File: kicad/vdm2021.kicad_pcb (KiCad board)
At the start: 2 copper layers, 254 x 134.1 mm, 177 parts, among them IC1 7406, IC10 74LS109, IC11 74LS138, IC12 74LS86, IC13 74LS109, IC14 74LS02, IC15 74LS00, IC16 74LS109, IC17 74LS175, IC18 74LS132, IC19 74LS04, IC2 74LS163, IC20 74LS163, IC21 74LS163, IC22 74LS163, IC23 74LS157, IC24 74LS157, IC25 4049, IC26 4029, IC27 4029, IC28 74LS157, IC29 DM8131, IC3 74166, IC30 4001, IC31 4042, IC32 4042, IC33 74LS08, IC34 74LS08, IC35 74LS00, IC36 74LS04, IC37 8836, IC38 74LS367, IC39 74LS367, IC4 MCM6575, IC40 74LS10, IC41 2102, IC42 2102, IC43 2102, IC44 2102, IC45 2102, IC46 2102, IC47 2102, IC48 2102, IC49 L7805, IC5 74LS175, IC50 L7812, IC6 74LS175, IC7 74LS20, IC8 93L16, IC9 74LS10, J2 Jumper_3_Open, J4 Jumper_2_Open, J5 Jumper_2_Open, Q1 2N2907, SW1 SW_DIP_x06, Y1 Crystal

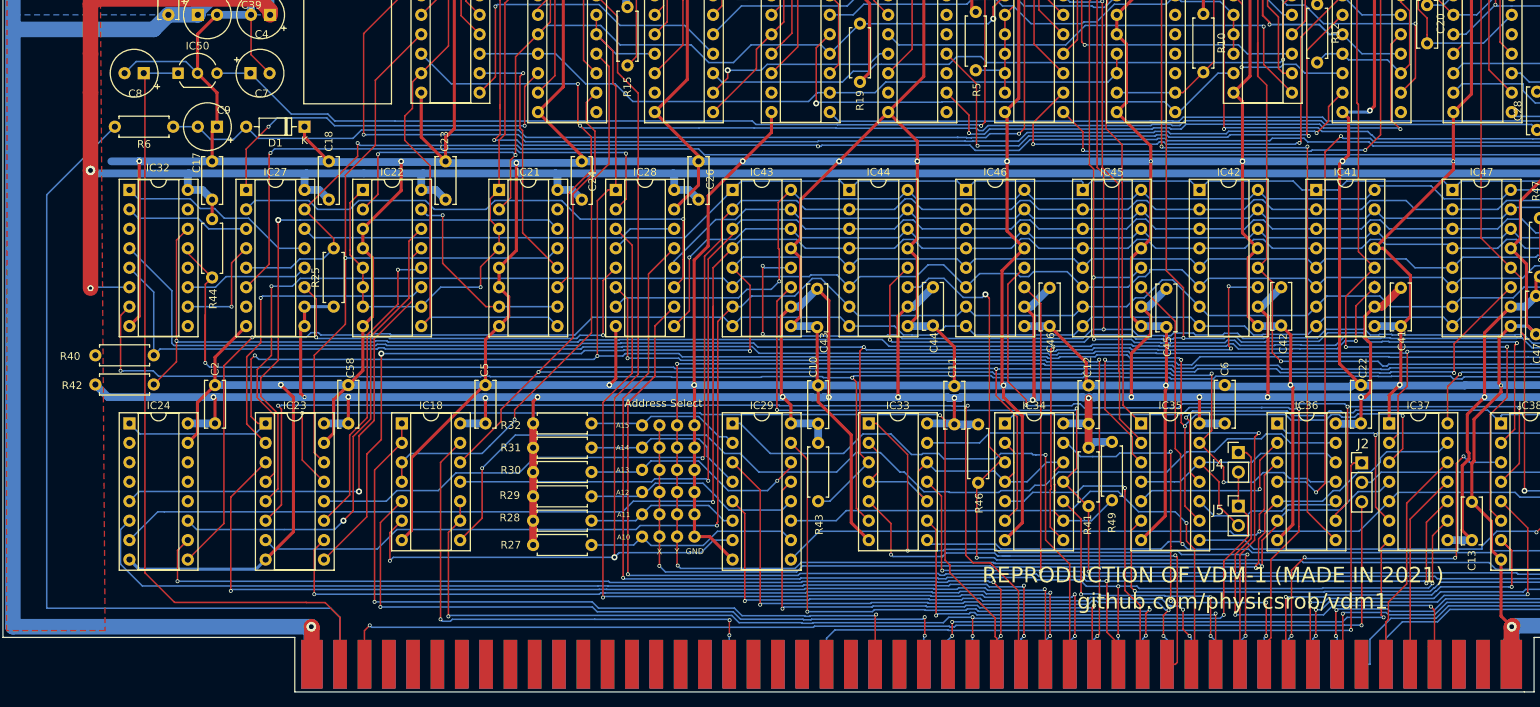
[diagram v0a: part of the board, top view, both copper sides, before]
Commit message: Updated silkscreen URL.  Increased footprint size of R6 half watt resistor
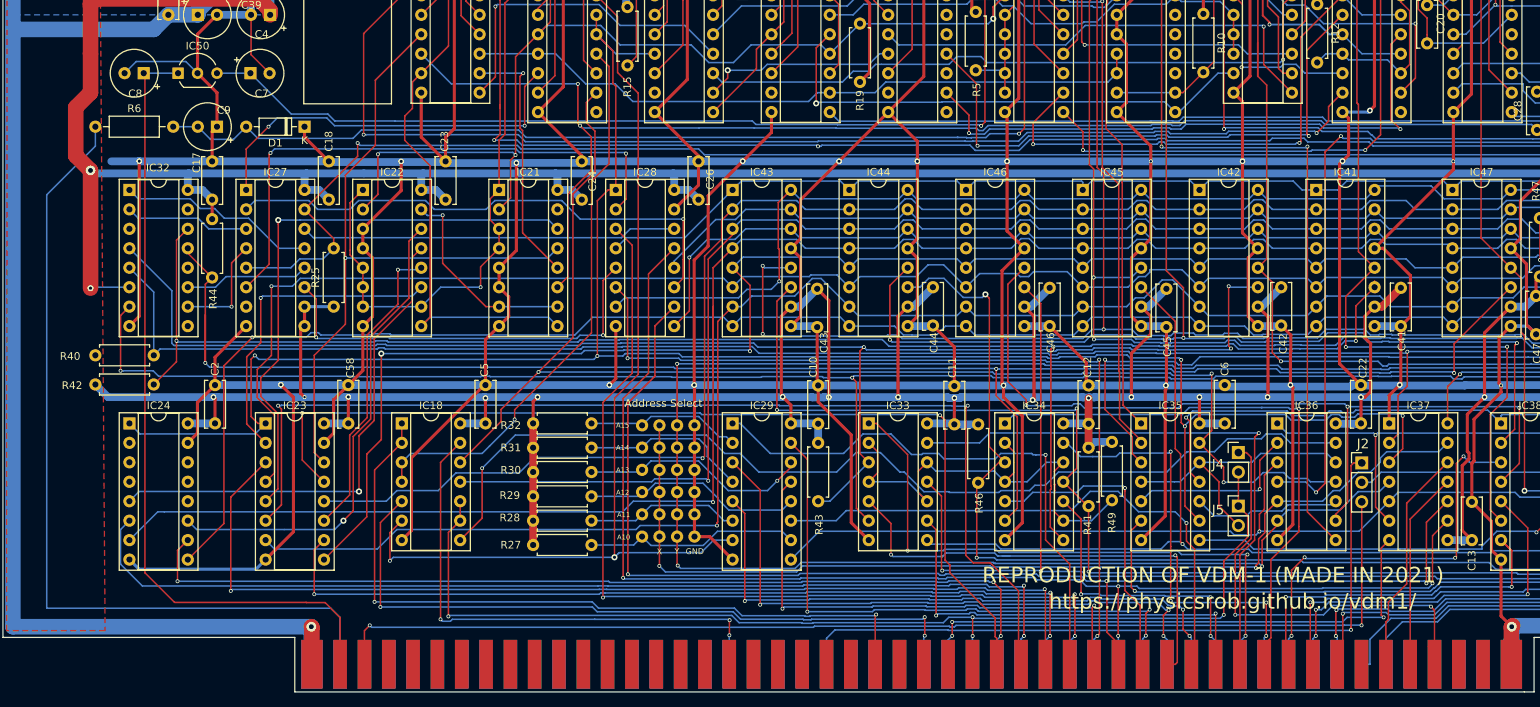
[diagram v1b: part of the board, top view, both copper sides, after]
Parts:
- R6: footprint Resistor_THT:R_Axial_DIN0207_L6.3mm_D2.5mm_P7.62mm_Horizontal -> Resistor_THT:R_Axial_DIN0207_L6.3mm_D2.5mm_P10.16mm_Horizontal
- moved R6 2.54 mm to (29.8, 78.1)
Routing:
- net +5V: track 1725.7 -> 1727.3 mm
- net Net-(R6-Pad1): track 111.5 -> 110.4 mm
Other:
- board text added: "https://physicsrob.github.io/vdm1/"
- board text removed: "github.com/physicsrob/vdm1"
